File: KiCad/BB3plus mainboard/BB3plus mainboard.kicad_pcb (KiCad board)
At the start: 4 copper layers, 233 x 230.5 mm, 420 parts, among them IC1 M24C32-DFDW6TP, IC10 THVD1420DR, IC11 TPD4E001DRLR, IC12 TPD4E001DRLR, IC13 USB5807C/KD, IC14 TPS62933ODRLR, IC15 MIC2026A-1YM-TR, IC16 PTN5150AHXMP, IC17 TPS2068E, IC18 TPD2E001DRLR, IC19 TPD2E001DRLR, IC2 TPS3851H18EDRBR, IC20 FUSB340TMX, IC21 TPS22948DCKR, IC22 SN74LVC1G3157DCK, IC23 LMK1C1106APWR, IC24 SN74LVC1G3157DCK, IC25 TLE75008ESDXUMA1, IC3 STM32G071RBT6, IC4 SN74HCS02PWR, IC5 TPS62933ODRLR, IC6 LM64460CPPQRYFRQ1, IC7 EMC2301-1-ACZL-TR, IC8 ISO6763FDWR, IC9 BD00FC0W, K1 AZ943-1CH-12DE, K2 AZ943-1CH-12DE, K3 RT424012, K4 RT424012, K5 RT424012, K6 RT424012, K7 RT424012, Q1 2N7002, Q2 2N7002, Q3 2N7002, Q4 2N7002, Q5 MMBT5401, Q6 DMP3013SFV-7, Q7 2N7002, Q8 2N7002, SW1 WBL2UOAGQR05CLR, SW2 PEC16-2215F-S0024, X1 DF40HC(3.0)-100DS-0.4V(51), X10 B3P-VH-FB-B, X11 B3P-VH-FB-B, X12 B3P-VH-FB-B, X13 22-27-2031, X14 TBP03R1-350-10BE, X15 USB4080-03-A, X16 MGB0A1-1CDDB005H, X17 SS-53000-002, X18 505110-2291, X19 505110-2291, X2 DF40HC(3.0)-100DS-0.4V(51), X20 10018783-10101TLF, X21 10018783-10101TLF, X22 10018783-10101TLF, X23 10018783-10101TLF, X24 10018783-10101TLF, X25 PH2-20-UA, X26 PH2-20-UA, X27 TBP03R1-350-10BE, X28 PH2-20-UA, X3 SM3ZS067U410AMR1000, X5 571-0400, X6 GSP1.9101.1, X7 1-726388-2, X8 B3P-VH-FB-B, X9 22-23-2031, Y1 FC-135 32.7680KA-K0, Y2 VXM7-9032-25M0000000, Y3 ECS-TXO-32CSMV-100-AN-TR

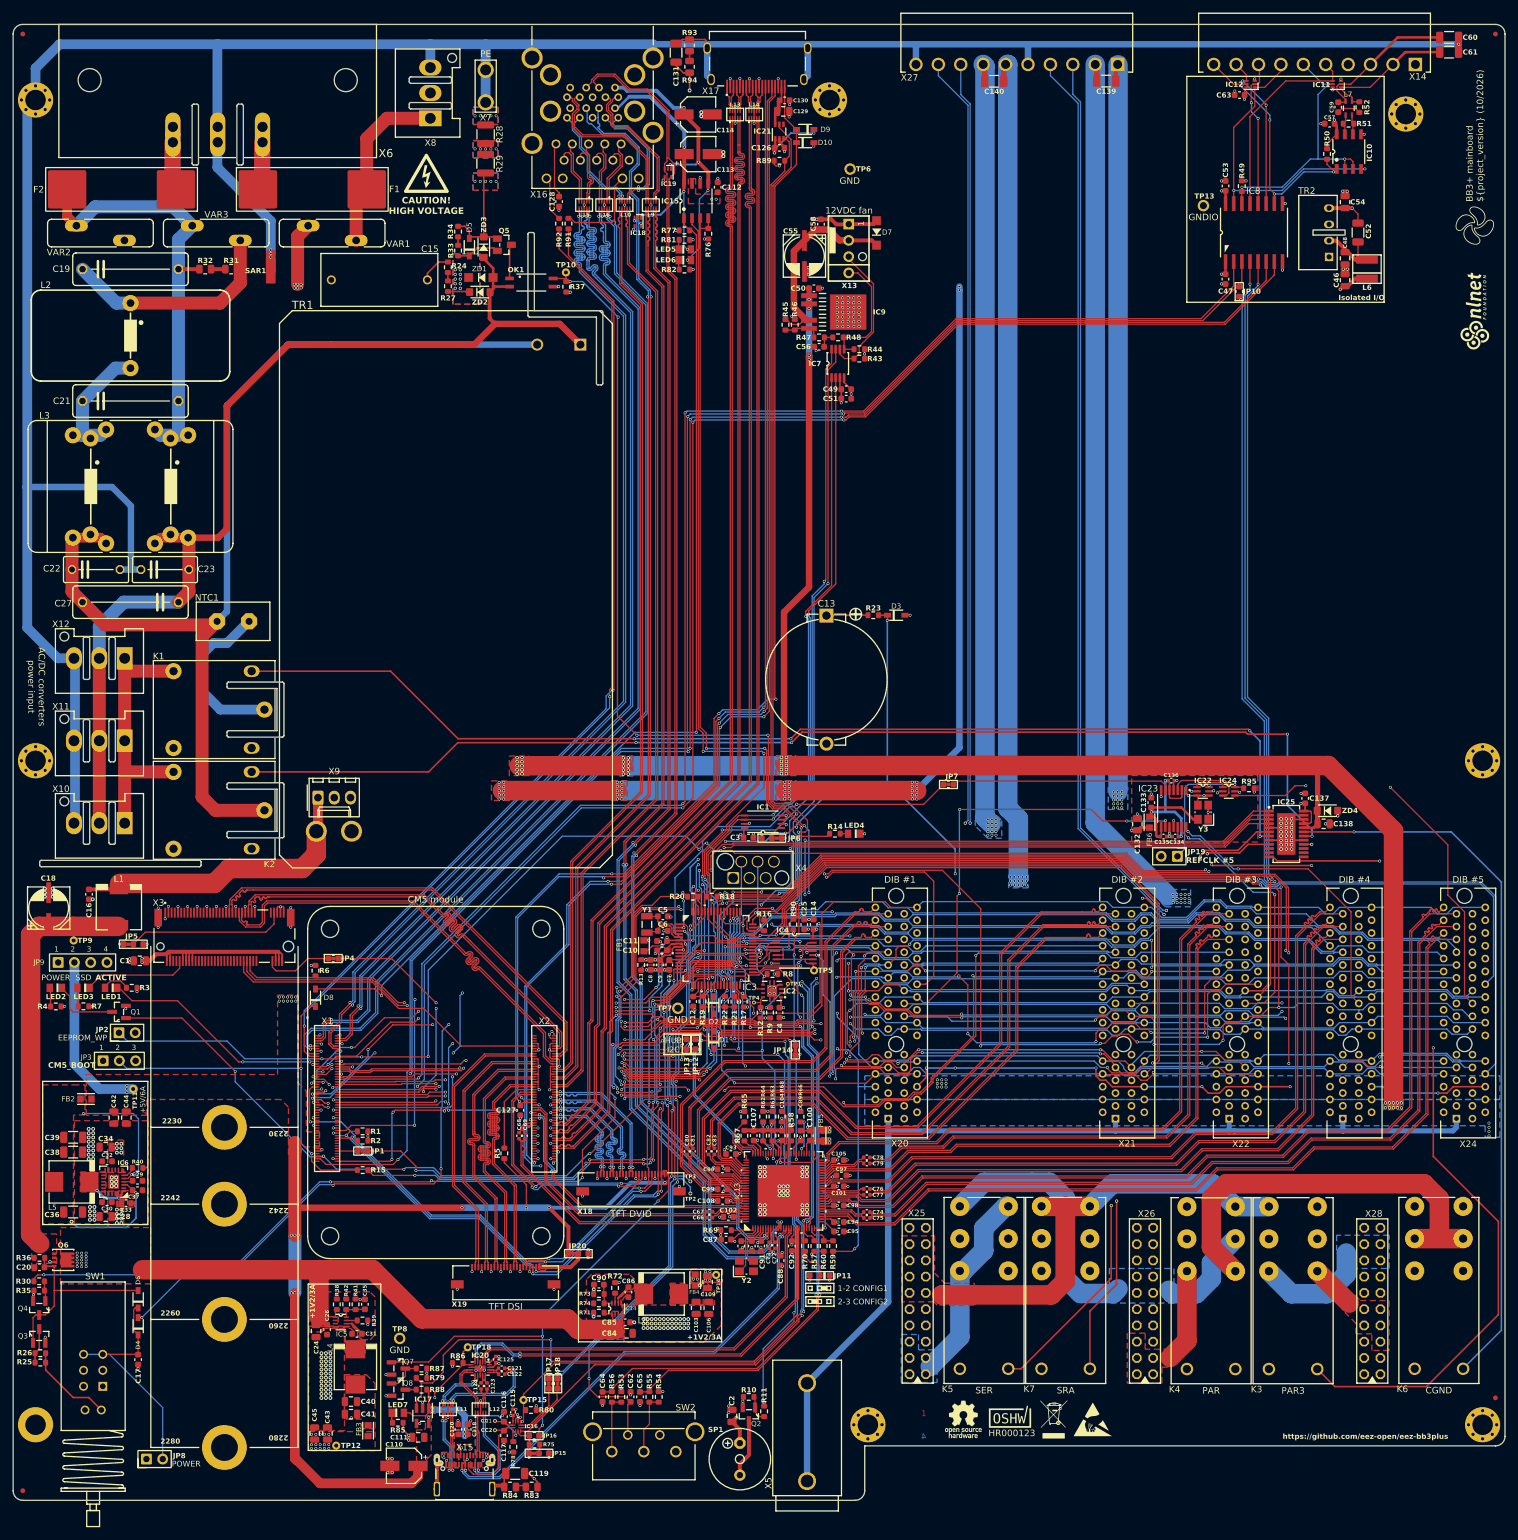
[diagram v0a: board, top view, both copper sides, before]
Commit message: SW1 footprint expanded
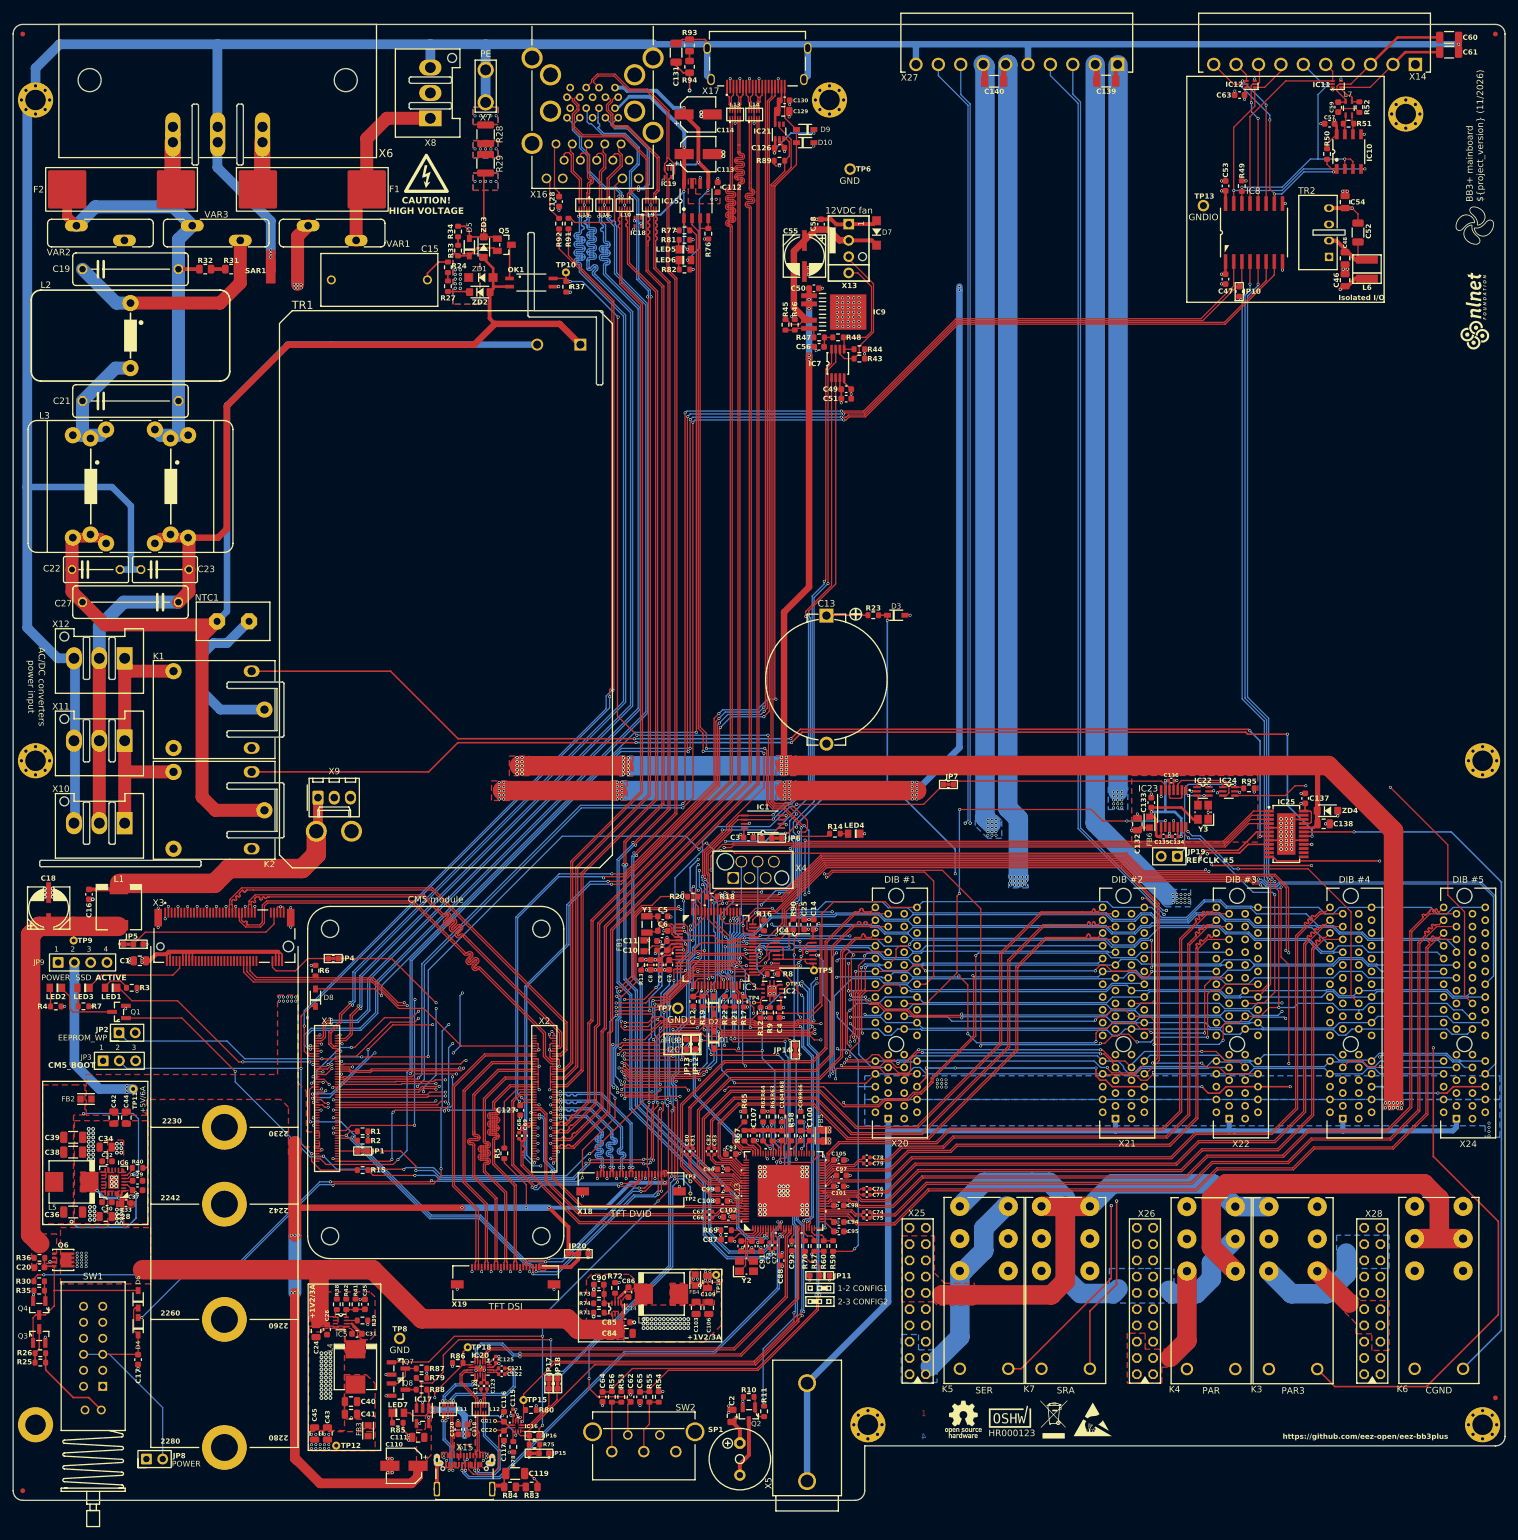
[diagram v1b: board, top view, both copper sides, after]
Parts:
- SW1: footprint PCM_EEZ_unsorted:WBL2UOAGQR05CLR -> PCM_EEZ_unsorted:WBL2UOAGQR05CLR_2
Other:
- board text added: "BB3+ mainboard ${project_version} (11/2026)"
- board text removed: "BB3+ mainboard ${project_version} (10/2026)"
